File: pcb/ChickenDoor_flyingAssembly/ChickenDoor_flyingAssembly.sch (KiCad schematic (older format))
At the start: 5 parts

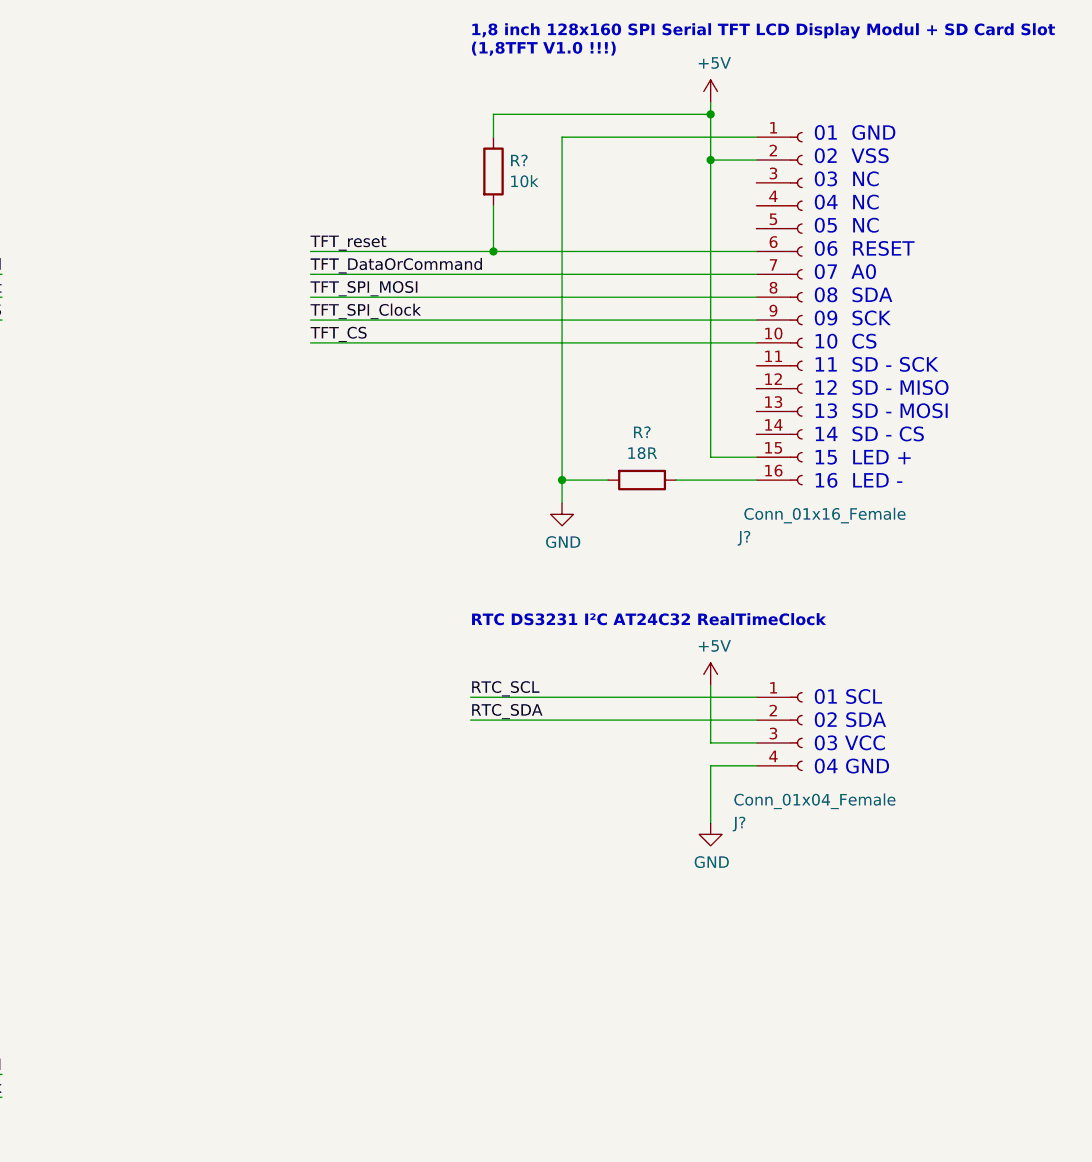
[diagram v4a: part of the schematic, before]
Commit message: Implemented a EnergySavingMaster and embedded to the software. Currently used for the backlight dimming after a certain time. (Much work for little feature)
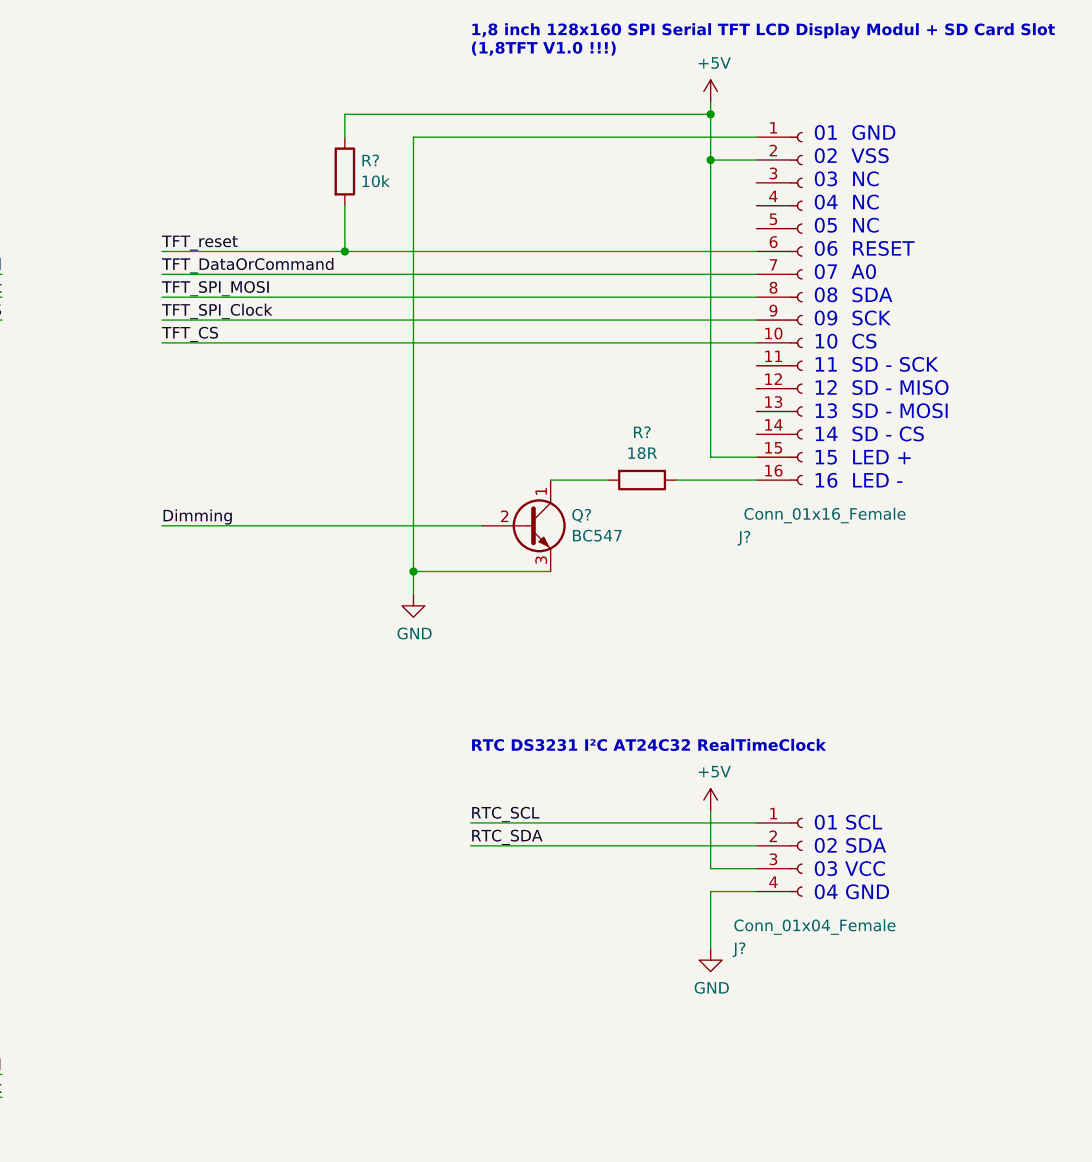
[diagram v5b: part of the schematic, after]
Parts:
- added Q?: BC547, Package_TO_SOT_THT:TO-92_Inline, symbol Transistor_BJT:BC547
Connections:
- net GND: now also Q?.3 (E); no longer R?.2
- new net: Q?.1 (C), R?.2
- new net Dimming: Q?.2 (B)
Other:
- moved on the sheet: J?, R?
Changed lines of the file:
@@
 L power:GND #PWR?
 U 1 1 5EDDCCDC
-P 8350 3200
-F 0 "#PWR?" H 8350 2950 50  0001 C CNN
-F 1 "GND" H 8355 3027 50  0000 C CNN
-F 2 "" H 8350 3200 50  0001 C CNN
-F 3 "" H 8350 3200 50  0001 C CNN
-	1    8350 3200
-	1    0    0    -1
-$EndComp
-Wire Wire Line
-	8350 3200 8350 3100
-Wire Wire Line
-	8350 3100 8550 3100
-Wire Wire Line
-	8350 3100 8350 1600
-Wire Wire Line
-	8350 1600 9200 1600
+P 7700 3600
+F 0 "#PWR?" H 7700 3350 50  0001 C CNN
+F 1 "GND" H 7705 3427 50  0000 C CNN
+F 2 "" H 7700 3600 50  0001 C CNN
+F 3 "" H 7700 3600 50  0001 C CNN
+	1    7700 3600
+	1    0    0    -1
+$EndComp
+Wire Wire Line
+	7700 3600 7700 3500
+Wire Wire Line
+	7700 3500 8300 3500
+Wire Wire Line
+	7700 3500 7700 1600
+Wire Wire Line
+	7700 1600 9200 1600
 $Comp
 L power:+3V3 #PWR?
@@
 Wire Wire Line
 	2050 5500 2050 5450
-Connection ~ 8350 3100
+Connection ~ 7700 3500
 Text Notes 9450 3150 0    63   ~ 0
 01  GND\n02  VSS\n03  NC\n04  NC\n05  NC\n06  RESET\n07  A0\n08  SDA\n09  SCK\n10  CS\n11  SD - SCK\n12  SD - MISO\n13  SD - MOSI\n14  SD - CS\n15  LED +\n16  LED -
@@
 	9200 3000 9000 3000
 Wire Wire Line
-	9200 2100 8050 2100
-Wire Wire Line
-	9200 2200 7250 2200
-Wire Wire Line
-	9200 2300 7250 2300
-Wire Wire Line
-	9200 2400 7250 2400
-Wire Wire Line
-	9200 2500 7250 2500
-Text Label 7250 2100 0    50   ~ 0
+	9200 2100 7400 2100
+Wire Wire Line
+	9200 2200 6600 2200
+Wire Wire Line
+	9200 2300 6600 2300
+Wire Wire Line
+	9200 2400 6600 2400
+Wire Wire Line
+	9200 2500 6600 2500
+Text Label 6600 2100 0    50   ~ 0
 TFT_reset
-Text Label 7250 2200 0    50   ~ 0
+Text Label 6600 2200 0    50   ~ 0
 TFT_DataOrCommand
-Text Label 7250 2300 0    50   ~ 0
+Text Label 6600 2300 0    50   ~ 0
 TFT_SPI_MOSI
-Text Label 7250 2400 0    50   ~ 0
+Text Label 6600 2400 0    50   ~ 0
 TFT_SPI_Clock
-Text Label 7250 2500 0    50   ~ 0
+Text Label 6600 2500 0    50   ~ 0
 TFT_CS
 Wire Wire Line
@@
 L Connector:Conn_01x04_Female J?
 U 1 1 5EE14116
-P 9400 4150
-F 0 "J?" H 9100 3700 50  0000 L CNN
-F 1 "Conn_01x04_Female" H 9100 3800 50  0000 L CNN
-F 2 "" H 9400 4150 50  0001 C CNN
-F 3 "~" H 9400 4150 50  0001 C CNN
-	1    9400 4150
-	1    0    0    -1
-$EndComp
-Text Notes 9450 4400 0    63   ~ 0
+P 9400 4700
+F 0 "J?" H 9100 4250 50  0000 L CNN
+F 1 "Conn_01x04_Female" H 9100 4350 50  0000 L CNN
+F 2 "" H 9400 4700 50  0001 C CNN
+F 3 "~" H 9400 4700 50  0001 C CNN
+	1    9400 4700
+	1    0    0    -1
+$EndComp
+Text Notes 9450 4950 0    63   ~ 0
 01 SCL\n02 SDA\n03 VCC\n04 GND
-Text Notes 7950 3750 0    50   ~ 10
+Text Notes 7950 4300 0    50   ~ 10
 RTC DS3231 I²C AT24C32 RealTimeClock
 $Comp
 L power:GND #PWR?
 U 1 1 5EE1931E
-P 9000 4600
-F 0 "#PWR?" H 9000 4350 50  0001 C CNN
-F 1 "GND" H 9005 4427 50  0000 C CNN
-F 2 "" H 9000 4600 50  0001 C CNN
-F 3 "" H 9000 4600 50  0001 C CNN
-	1    9000 4600
-	1    0    0    -1
-$EndComp
-Wire Wire Line
-	9200 4350 9000 4350
-Wire Wire Line
-	9000 4350 9000 4600
-Wire Wire Line
-	9200 4250 9000 4250
-Wire Wire Line
-	9000 4250 9000 4000
-Wire Wire Line
-	9200 4050 7950 4050
-Wire Wire Line
-	9200 4150 7950 4150
-Text Label 7950 4050 0    50   ~ 0
+P 9000 5150
+F 0 "#PWR?" H 9000 4900 50  0001 C CNN
+F 1 "GND" H 9005 4977 50  0000 C CNN
+F 2 "" H 9000 5150 50  0001 C CNN
+F 3 "" H 9000 5150 50  0001 C CNN
+	1    9000 5150
+	1    0    0    -1
+$EndComp
+Wire Wire Line
+	9200 4900 9000 4900
+Wire Wire Line
+	9000 4900 9000 5150
+Wire Wire Line
+	9200 4800 9000 4800
+Wire Wire Line
+	9000 4800 9000 4550
+Wire Wire Line
+	9200 4600 7950 4600
+Wire Wire Line
+	9200 4700 7950 4700
+Text Label 7950 4600 0    50   ~ 0
 RTC_SCL
-Text Label 7950 4150 0    50   ~ 0
+Text Label 7950 4700 0    50   ~ 0
 RTC_SDA
 Wire Wire Line
@@
 Wire Wire Line
 	2400 2400 1500 2400
-Wire Wire Line
-	9000 1450 9000 1500
 $Comp
 L Device:R R?
@@
 L power:+5V #PWR?
 U 1 1 5EE41E7D
-P 9000 4000
-F 0 "#PWR?" H 9000 3850 50  0001 C CNN
-F 1 "+5V" H 9015 4173 50  0000 C CNN
-F 2 "" H 9000 4000 50  0001 C CNN
-F 3 "" H 9000 4000 50  0001 C CNN
-	1    9000 4000
+P 9000 4550
+F 0 "#PWR?" H 9000 4400 50  0001 C CNN
+F 1 "+5V" H 9015 4723 50  0000 C CNN
+F 2 "" H 9000 4550 50  0001 C CNN
+F 3 "" H 9000 4550 50  0001 C CNN
+	1    9000 4550
 	1    0    0    -1
 $EndComp
@@
 L Device:R R?
 U 1 1 5EE6340C
-P 8050 1750
-F 0 "R?" H 8120 1796 50  0000 L CNN
-F 1 "10k" H 8120 1705 50  0000 L CNN
-F 2 "" V 7980 1750 50  0001 C CNN
-F 3 "~" H 8050 1750 50  0001 C CNN
-	1    8050 1750
-	1    0    0    -1
-$EndComp
-Wire Wire Line
-	9000 1500 8050 1500
-Wire Wire Line
-	8050 1500 8050 1600
-Connection ~ 9000 1500
-Wire Wire Line
-	9000 1500 9000 1700
-Wire Wire Line
-	8050 1900 8050 2100
-Connection ~ 8050 2100
-Wire Wire Line
-	8050 2100 7250 2100
+P 7400 1750
+F 0 "R?" H 7470 1796 50  0000 L CNN
+F 1 "10k" H 7470 1705 50  0000 L CNN
+F 2 "" V 7330 1750 50  0001 C CNN
+F 3 "~" H 7400 1750 50  0001 C CNN
+	1    7400 1750
+	1    0    0    -1
+$EndComp
+Wire Wire Line
+	9000 1500 7400 1500
+Wire Wire Line
+	7400 1500 7400 1600
+Wire Wire Line
+	7400 1900 7400 2100
+Connection ~ 7400 2100
+Wire Wire Line
+	7400 2100 6600 2100
 Text Notes 5300 3000 0    50   ~ 0
 D22 - back \nD24 - enter\nD26 - up\nD28 - down
+$Comp
+L Transistor_BJT:BC547 Q?
+U 1 1 5F443A1A
+P 8200 3300
+F 0 "Q?" H 8391 3346 50  0000 L CNN
+F 1 "BC547" H 8391 3255 50  0000 L CNN
+F 2 "Package_TO_SOT_THT:TO-92_Inline" H 8400 3225 50  0001 L CIN
+F 3 "http://www.fairchildsemi.com/ds/BC/BC547.pdf" H 8200 3300 50  0001 L CNN
+	1    8200 3300
+	1    0    0    -1
+$EndComp
+Wire Wire Line
+	9000 1450 9000 1500
+Connection ~ 9000 1500
+Wire Wire Line
+	9000 1500 9000 1700
+Wire Wire Line
+	8300 3100 8550 3100
+Wire Wire Line
+	8000 3300 6600 3300
+Text Label 6600 3300 0    50   ~ 0
+Dimming
 $EndSCHEMATC

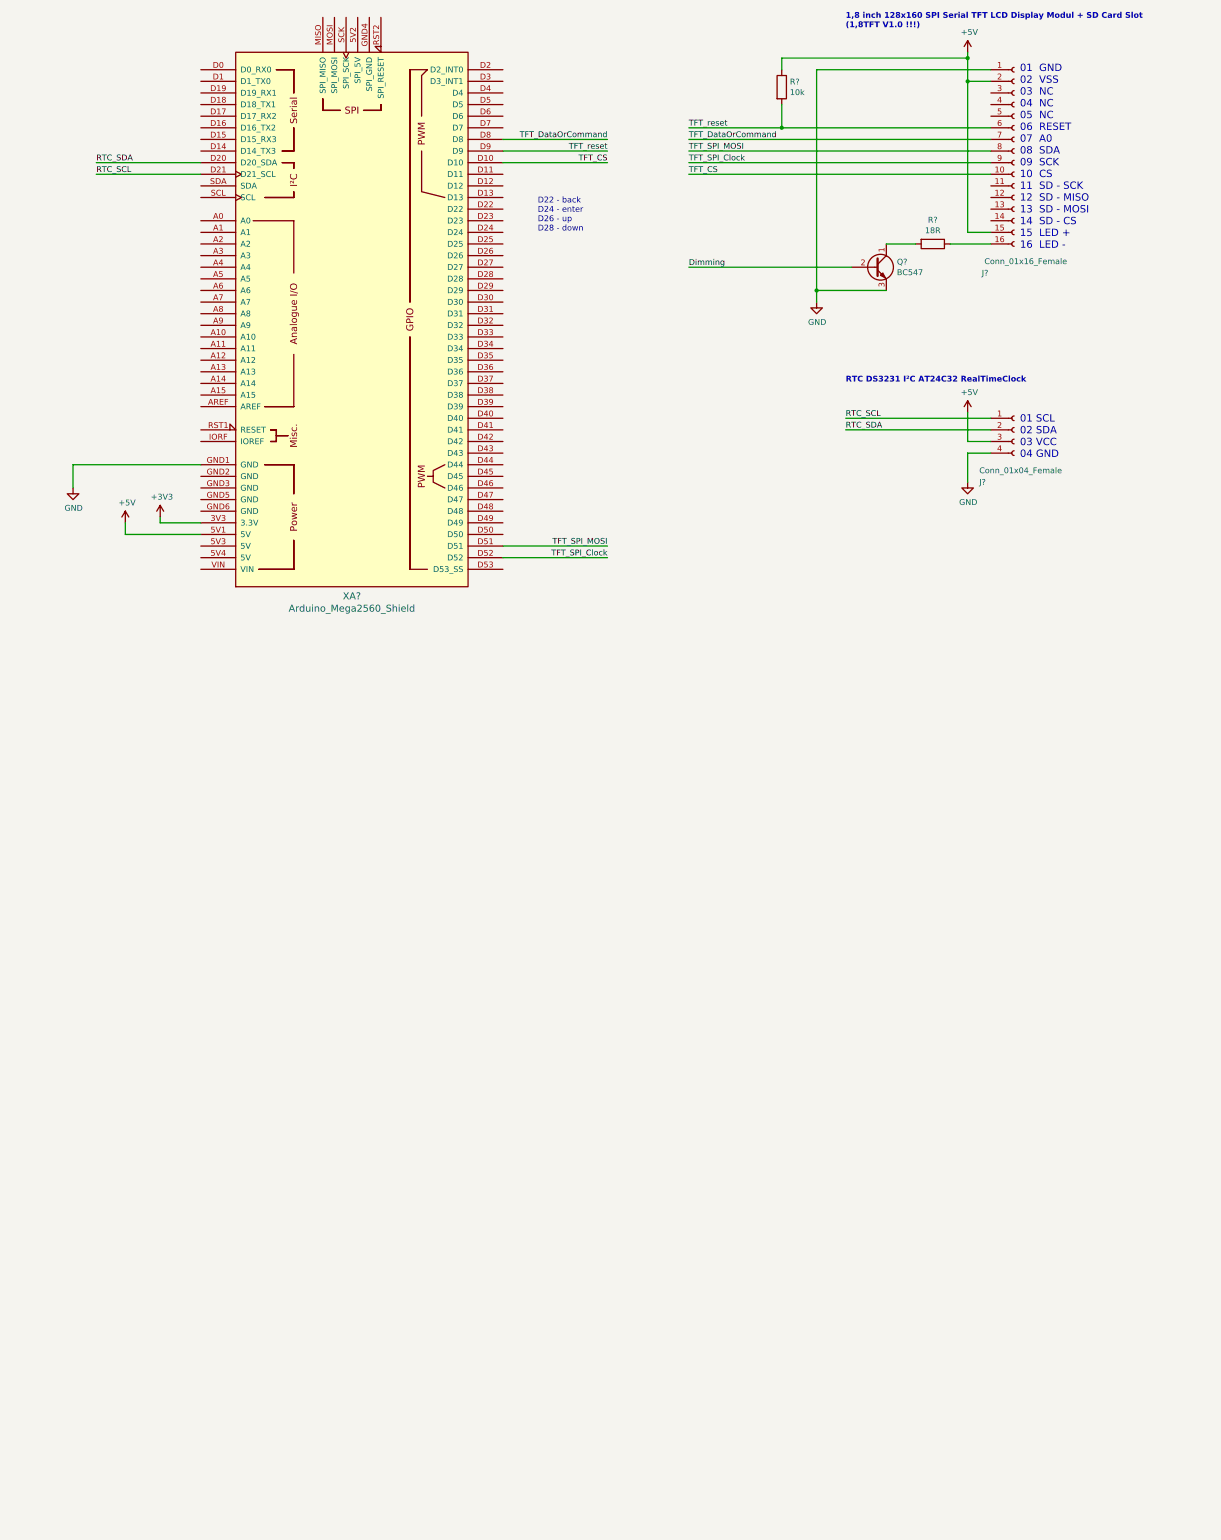
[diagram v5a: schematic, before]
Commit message: Updated the circuit diagram with new motor control
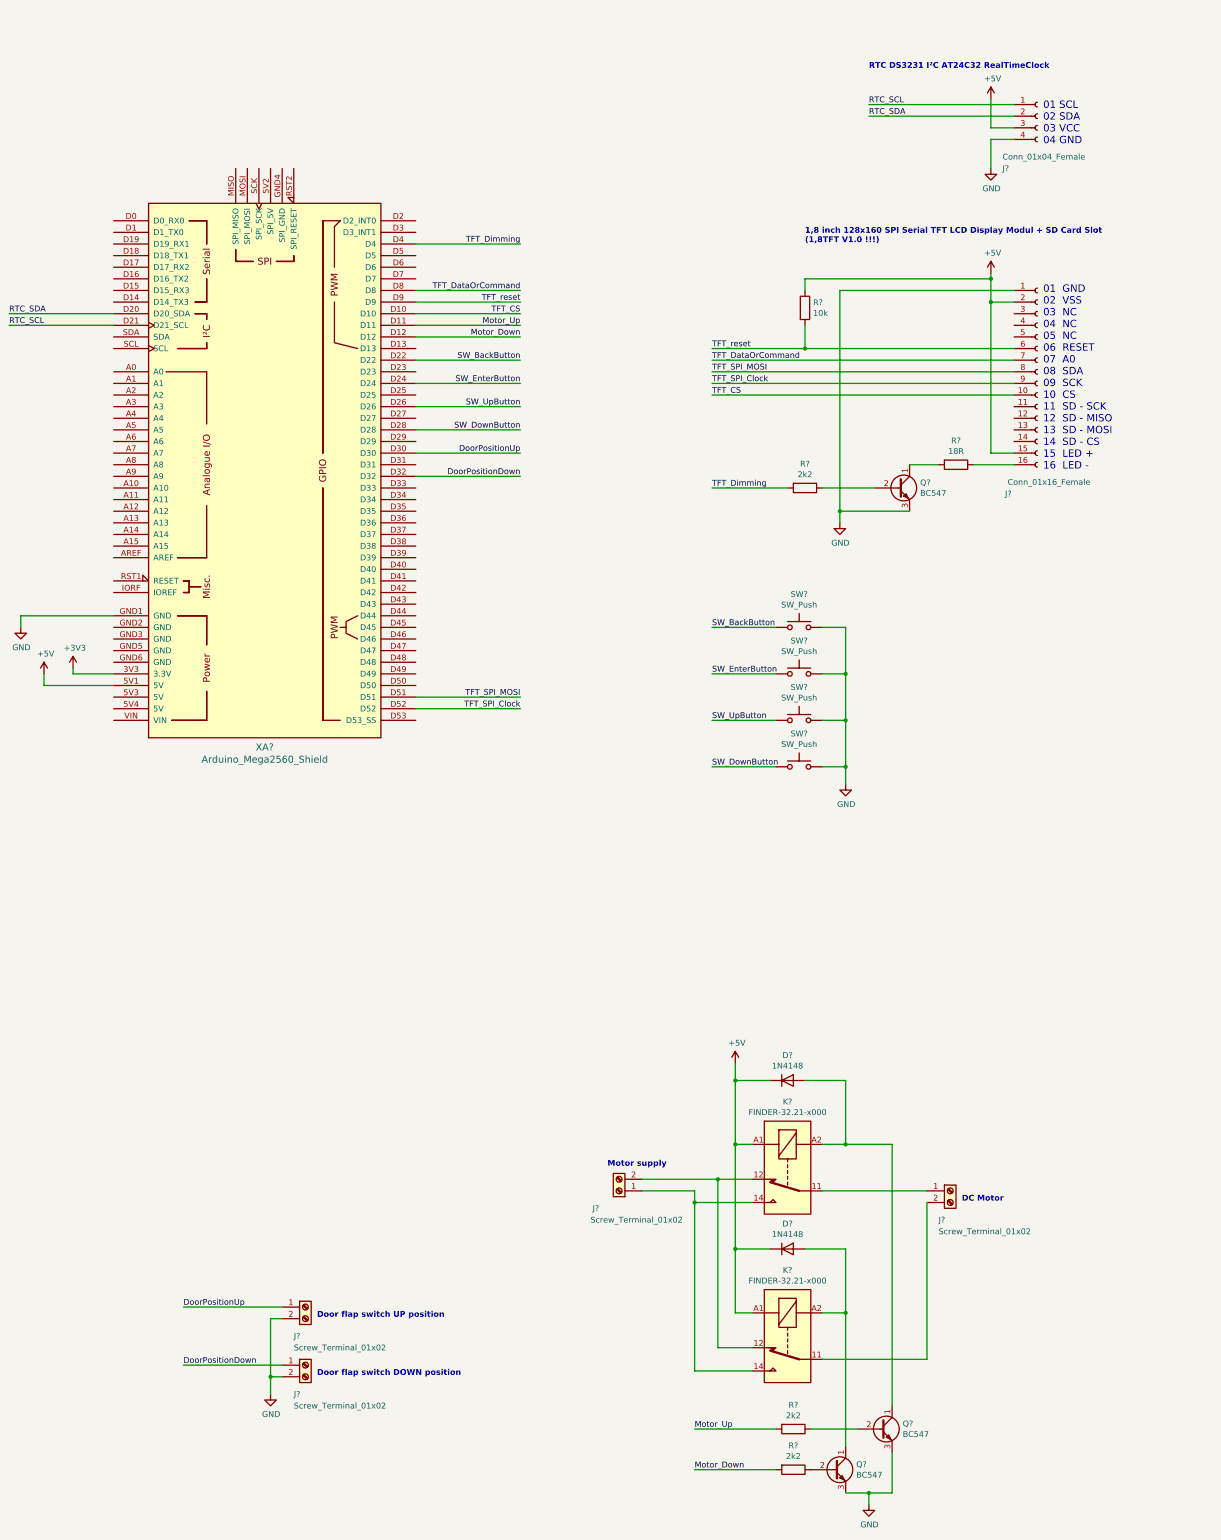
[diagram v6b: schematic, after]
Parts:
- added D? (x2): 1N4148, Diode_THT:D_DO-35_SOD27_P7.62mm_Horizontal, symbol Diode:1N4148
- added J? (x4): Screw_Terminal_01x02, symbol Connector:Screw_Terminal_01x02
- added K? (x2): FINDER-32.21-x000, Relay_THT:Relay_SPST_Finder_32.21-x300, symbol Relay:FINDER-32.21-x000
- added Q? (x2): BC547, Package_TO_SOT_THT:TO-92_Inline, symbol Transistor_BJT:BC547
- added R? (x3): 2k2, symbol Device:R
- added SW? (x4): SW_Push, symbol Switch:SW_Push
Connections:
- net +5V: now also D?.1 (K), D?.1 (K), K?.A1, K?.A1
- net GND: now also J?.2 (Pin_2), J?.2 (Pin_2), Q?.3 (E), Q?.3 (E), SW?.2, SW?.2, SW?.2, SW?.2
- net Motor_Up: now reaches XA?.D11
- net Motor_Up: now also R?.2
- net Motor_Down: now reaches XA?.D12
- net Motor_Down: now also R?.2
- net SW_BackButton: now reaches XA?.D22
- net SW_BackButton: now also SW?.1
- net SW_EnterButton: now reaches XA?.D24
- net SW_EnterButton: now also SW?.1
- net SW_UpButton: now reaches XA?.D26
- net SW_UpButton: now also SW?.1
- net SW_DownButton: now reaches XA?.D28
- net SW_DownButton: now also SW?.1
- net DoorPositionUp: now reaches XA?.D30
- net DoorPositionUp: now also J?.1 (Pin_1)
- net DoorPositionDown: now reaches XA?.D32
- net DoorPositionDown: now also J?.1 (Pin_1)
- net TFT_Dimming: now reaches XA?.D4
- net TFT_Dimming: now also R?.2
- net Dimming: no longer names the net of Q?.2 (B)
- net Dimming: now also R?.1
- new net: J?.1 (Pin_1), K?.11
- new net: J?.2 (Pin_2), K?.12, K?.12
- new net: J?.1 (Pin_1), K?.14, K?.14
- new net: D?.2 (A), K?.A2, Q?.1 (C) (x2)
- new net: J?.2 (Pin_2), K?.11
- new net: Q?.2 (B), R?.1 (x2)
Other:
- note added: "DC Motor"
- note added: "Door flap switch DOWN position"
- note added: "Door flap switch UP position"
- note added: "Motor supply"
- note removed: "D22 - back \nD24 - enter\nD26 - up\nD28 - down"
- moved on the sheet: J?, Q?, R?, XA?
